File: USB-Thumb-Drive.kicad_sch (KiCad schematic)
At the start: 5 parts, among them J101 USB_C_Receptacle_USB2.0_14P

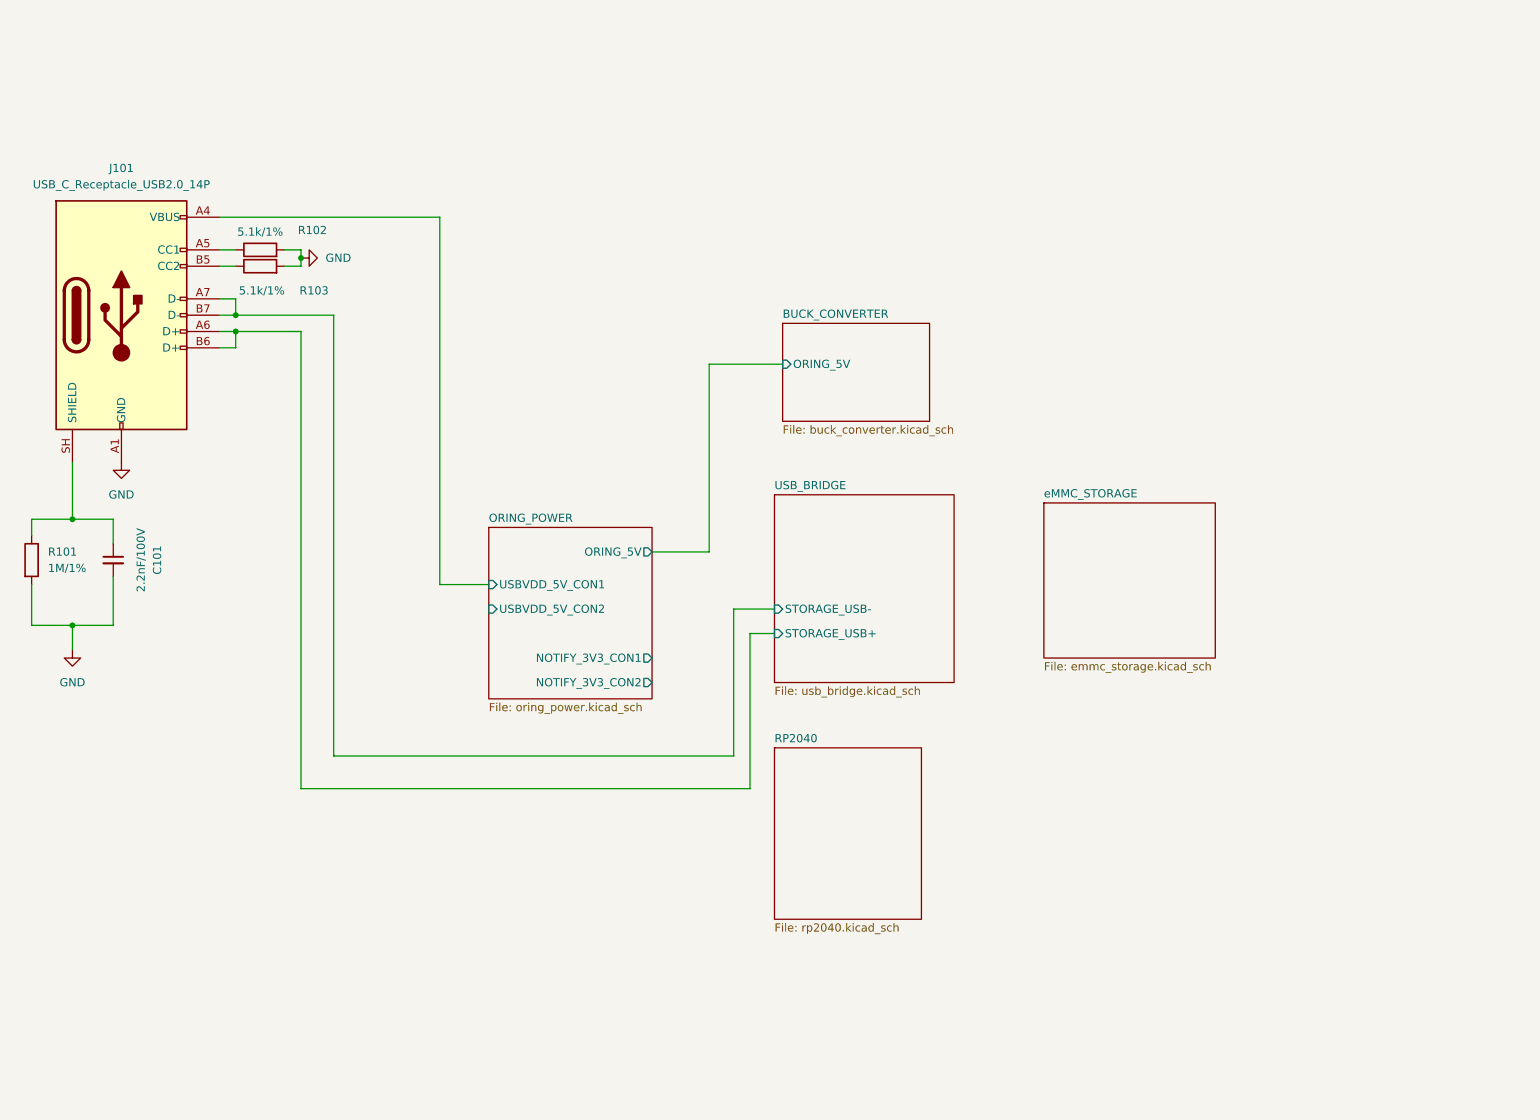
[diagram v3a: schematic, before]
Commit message: Progress RP2040 schematic
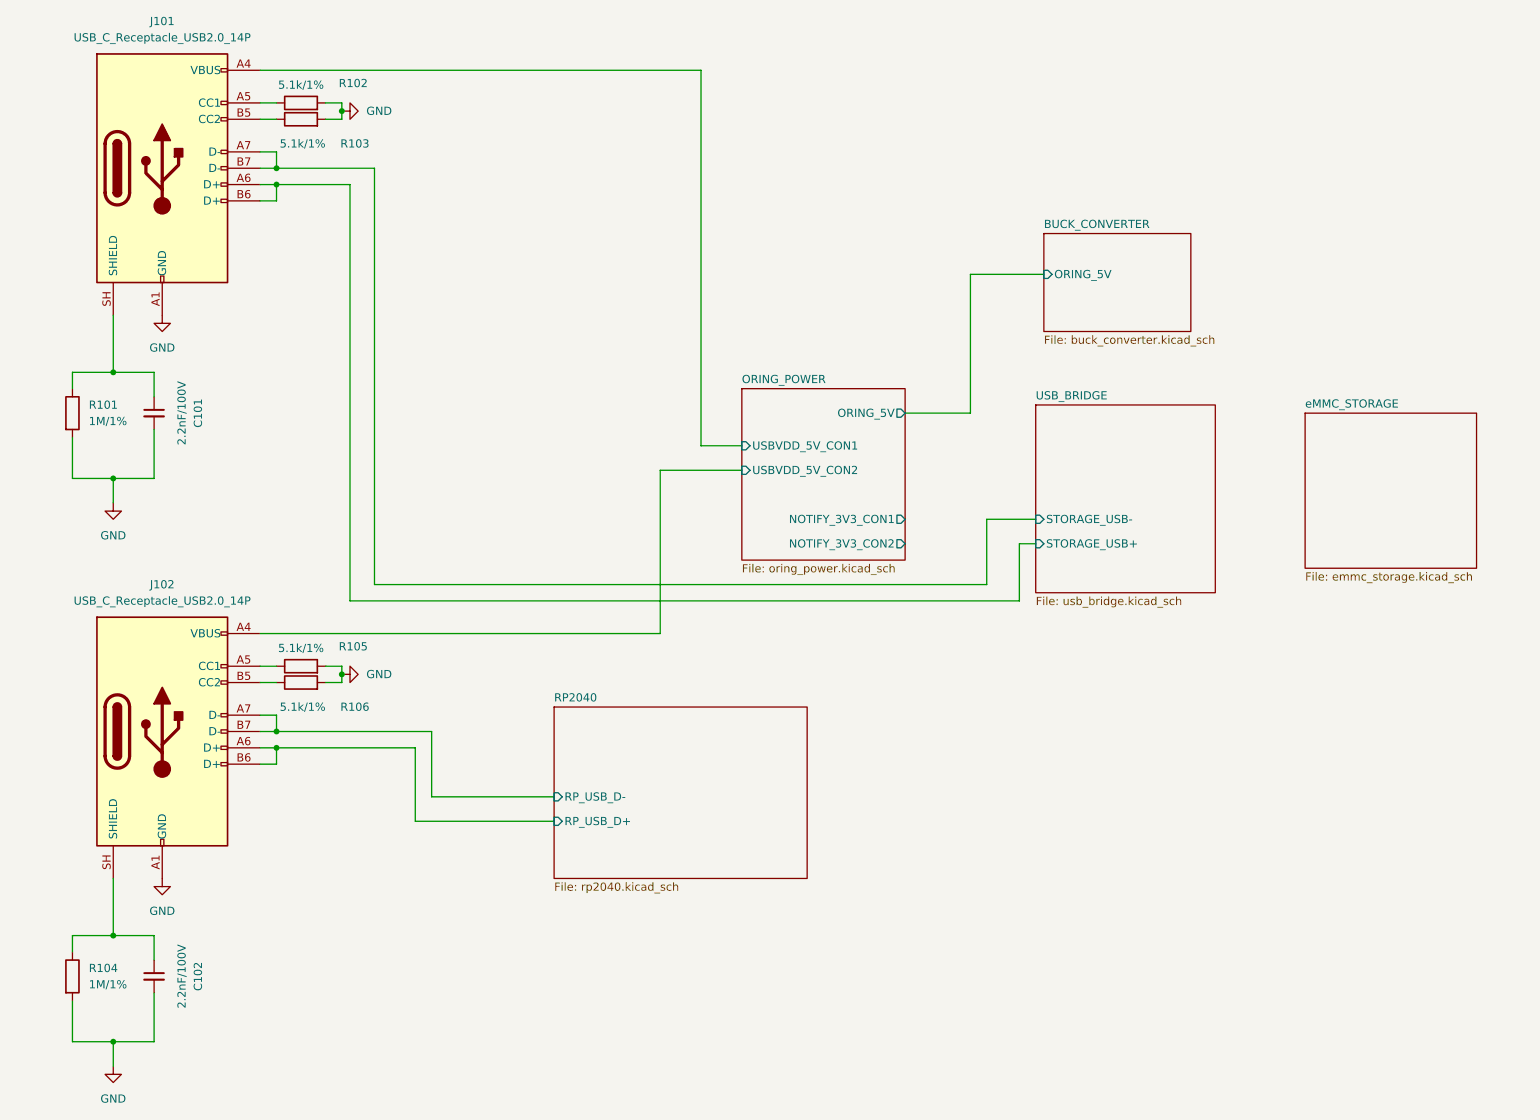
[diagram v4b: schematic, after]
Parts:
- added C102: 2.2nF/100V, SparkFun-Capacitor:C_0603_1608Metric, symbol SparkFun-Capacitor:C_Small
- added J102: USB_C_Receptacle_USB2.0_14P, Connector_USB:USB_C_Receptacle_XKB_U262-16XN-4BVC11, symbol Connector:USB_C_Receptacle_USB2.0_14P
- added R104: 1M/1%, Resistor_SMD:R_01005_0402Metric, symbol Device:R
- added R105, R106: 5.1k/1%, Resistor_SMD:R_01005_0402Metric, symbol Device:R
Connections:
- net GND: now also C102.2, J102.A1 (GND), J102.A12 (GND), J102.B1 (GND), J102.B12 (GND), R104.2, R105.2, R106.2
- net ORING_POWER/USBVDD_5V_CON2: now also J102.A4 (VBUS), J102.A9 (VBUS), J102.B4 (VBUS), J102.B9 (VBUS)
- new net: C102.1, J102.SH (SHIELD), R104.1
- new net: J102.A5 (CC1), R105.1
- new net: J102.B5 (CC2), R106.1
- new net RP2040/RP_USB_D+: J102.A6 (D+), J102.B6 (D+)
- new net RP2040/RP_USB_D-: J102.A7 (D-), J102.B7 (D-)
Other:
- sheet RP2040 ports: added RP_USB_D+, RP_USB_D-; removed none
- moved on the sheet: C101, J101, R101, R102, R103
